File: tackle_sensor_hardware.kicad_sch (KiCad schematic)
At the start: 77 parts, among them J1 Conn_ARM_JTAG_SWD_10, J2 Conn_01x02_Male, J4 Conn_01x04_Male, J5 Conn_01x06_Male, Q1 DMP4051LK3, Q2 NCE0110K, SW1 PTS645SL43SMTR92 LFS, T1 DRQ125-330-R, U1 STM32G031Fx, U2 LM3488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

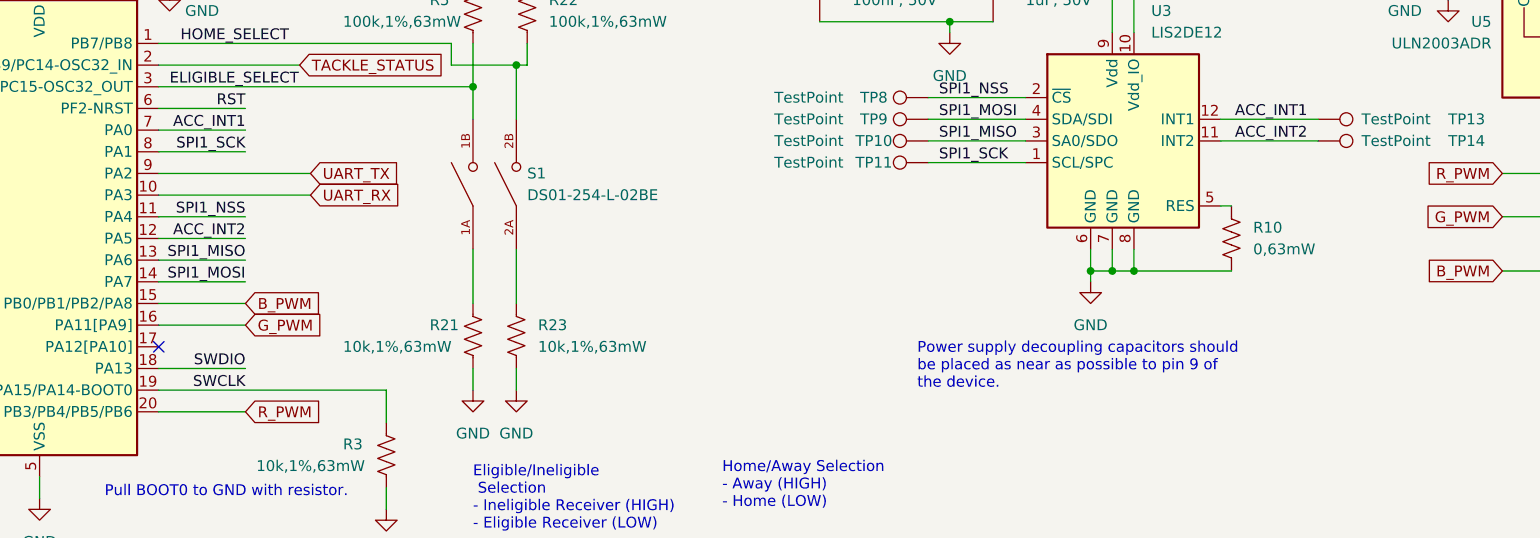
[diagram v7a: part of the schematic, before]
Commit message: - Change SPI RST to pull down to 10k.  Added line from MCU to toggle the ACCEL reset.  Added release files REV2
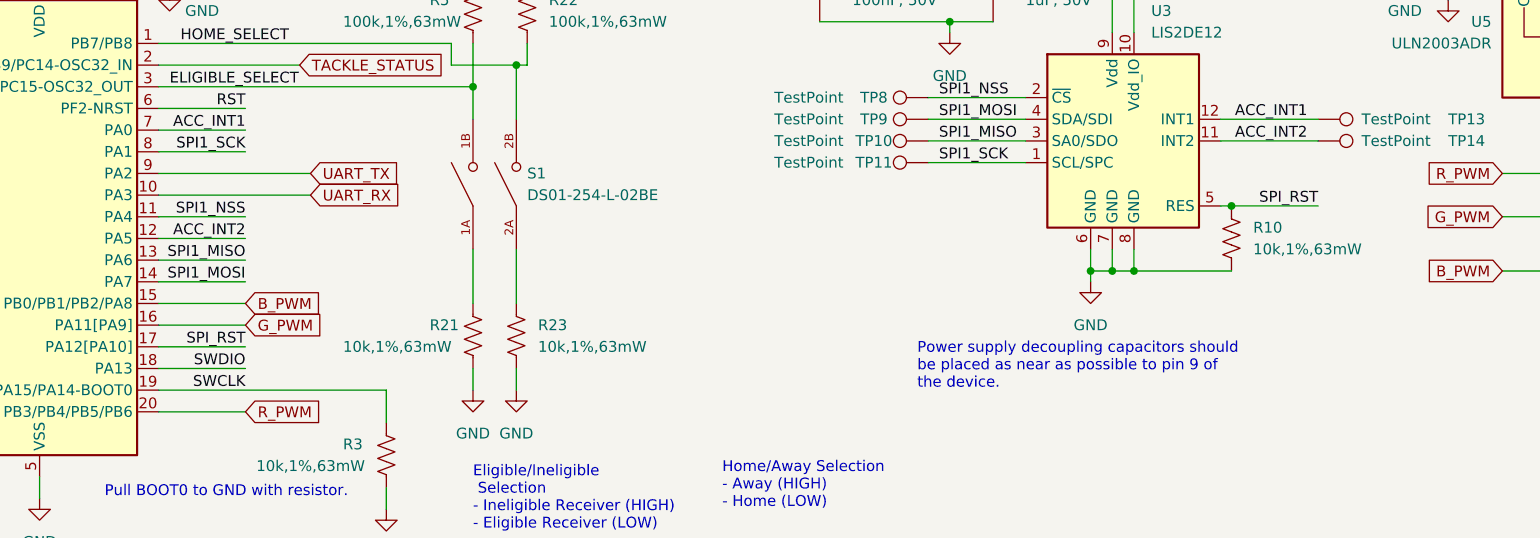
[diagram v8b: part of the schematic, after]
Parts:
- R10: value 0,63mW -> 10k,1%,63mW; JLCPN C106231 -> C25744; MPN RC0402FR-070RL -> 0402WGF1002TCE
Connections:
- net SPI_RST: now reaches R10.1, U3.5 (RES)
- net SPI_RST: now also U1.17 (PA12[PA10])
- no-connect marks 4 -> 3
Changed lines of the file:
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@@
   (junction (at 92.71 93.98) (diameter 0) (color 0 0 0 0)
   )
+  (junction (at 223.52 161.29) (diameter 0) (color 0 0 0 0)
+  )
   (junction (at 113.03 93.98) (diameter 0) (color 0 0 0 0)
   )
@@
   (no_connect (at 38.1 156.21))
   (no_connect (at 38.1 153.67))
-  (no_connect (at 97.79 177.8))
   (wire (pts (xy 119.38 93.98) (xy 119.38 85.09))
     (stroke (width 0) (type default) (color 0 0 0 0))
@@
     (stroke (width 0) (type default) (color 0 0 0 0))
   )
+  (wire (pts (xy 97.79 177.8) (xy 107.95 177.8))
+    (stroke (width 0) (type default) (color 0 0 0 0))
+  )
   (wire (pts (xy 97.79 180.34) (xy 107.95 180.34))
     (stroke (width 0) (type default) (color 0 0 0 0))
@@
     (stroke (width 0) (type default) (color 0 0 0 0))
   )
+  (wire (pts (xy 223.52 161.29) (xy 233.68 161.29))
+    (stroke (width 0) (type default) (color 0 0 0 0))
+  )
   (wire (pts (xy 88.9 128.27) (xy 83.82 128.27))
     (stroke (width 0) (type default) (color 0 0 0 0))
@@
     (effects (font (size 1.27 1.27)) (justify right bottom))
   )
+  (label "SPI_RST" (at 107.95 177.8 180)
+    (effects (font (size 1.27 1.27)) (justify right bottom))
+  )
   (label "SWDIO" (at 39.37 151.13 0)
     (effects (font (size 1.27 1.27)) (justify left bottom))
@@
     (effects (font (size 1.27 1.27)) (justify right bottom))
   )
+  (label "SPI_RST" (at 233.68 161.29 180)
+    (effects (font (size 1.27 1.27)) (justify right bottom))
+  )
   (label "SPI1_MOSI" (at 107.95 170.18 180)
     (effects (font (size 1.27 1.27)) (justify right bottom))
@@
     )
   )
+  (symbol (lib_id "Device:R_US") (at 223.52 165.1 0) (unit 1)
+    (in_bom yes) (on_board yes)
+    (property "Reference" "R10" (id 0) (at 226.06 163.83 0)
+      (effects (font (size 1.27 1.27)) (justify left))
+    )
+    (property "Value" "10k,1%,63mW" (id 1) (at 226.06 166.37 0)
+      (effects (font (size 1.27 1.27)) (justify left))
+    )
+    (property "Footprint" "Resistor_SMD:R_0402_1005Metric" (id 2) (at 224.536 165.354 90)
+      (effects (font (size 1.27 1.27)) hide)
+    )
+    (property "Datasheet" "https://datasheet.lcsc.com/lcsc/2206010100_UNI-ROYAL-Uniroyal-Elec-0402WGF1002TCE_C25744.pdf" (id 3) (at 223.52 165.1 0)
+      (effects (font (size 1.27 1.27)) hide)
+    )
+    (property "JLCPN" " C25744" (id 4) (at 223.52 165.1 0)
+      (effects (font (size 1.27 1.27)) hide)
+    )
+    (property "MPN" "0402WGF1002TCE" (id 5) (at 223.52 165.1 0)
+      (effects (font (size 1.27 1.27)) hide)
+    )
+    (pin "1")
+    (pin "2")
+  )
   (symbol (lib_id "Connector:TestPoint") (at 39.37 143.51 0) (unit 1)
     (in_bom yes) (on_board yes)
@@
     (pin "2")
   )
-  (symbol (lib_id "Device:R_US") (at 223.52 165.1 0) (unit 1)
-    (in_bom yes) (on_board yes) (fields_autoplaced)
-    (property "Reference" "R10" (id 0) (at 226.06 163.8299 0)
-      (effects (font (size 1.27 1.27)) (justify left))
-    )
-    (property "Value" "0,63mW" (id 1) (at 226.06 166.3699 0)
-      (effects (font (size 1.27 1.27)) (justify left))
-    )
-    (property "Footprint" "Resistor_SMD:R_0402_1005Metric" (id 2) (at 224.536 165.354 90)
-      (effects (font (size 1.27 1.27)) hide)
-    )
-    (property "Datasheet" "https://datasheet.lcsc.com/lcsc/1809291220_YAGEO-RC0402FR-070RL_C106231.pdf" (id 3) (at 223.52 165.1 0)
-      (effects (font (size 1.27 1.27)) hide)
-    )
-    (property "MPN" "RC0402FR-070RL" (id 4) (at 223.52 165.1 0)
-      (effects (font (size 1.27 1.27)) hide)
-    )
-    (property "JLCPN" "C106231" (id 5) (at 223.52 165.1 0)
-      (effects (font (size 1.27 1.27)) hide)
-    )
-    (pin "1")
-    (pin "2")
-  )
   (symbol (lib_id "Connector:TestPoint") (at 203.2 45.72 0) (unit 1)
     (in_bom yes) (on_board yes) (fields_autoplaced)
@@
       (reference "R9") (unit 1) (value "10k,1%,63mW") (footprint "Resistor_SMD:R_0402_1005Metric")
     )
-    (path "/cecdbddf-e2d3-491b-9b23-9ebcaeab9e47"
-      (reference "R10") (unit 1) (value "0,63mW") (footprint "Resistor_SMD:R_0402_1005Metric")
+    (path "/92367d55-e866-4d69-84fa-bb361751d6c6"
+      (reference "R10") (unit 1) (value "10k,1%,63mW") (footprint "Resistor_SMD:R_0402_1005Metric")
     )
     (path "/b84e7bb0-54b7-4489-9c51-6f984f4de541"
